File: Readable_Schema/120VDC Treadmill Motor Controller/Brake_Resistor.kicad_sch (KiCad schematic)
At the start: 11 parts, among them Q9 IPP200N25N3GXKSA1, U10 FOD3182, U11 TC75S56F_LF

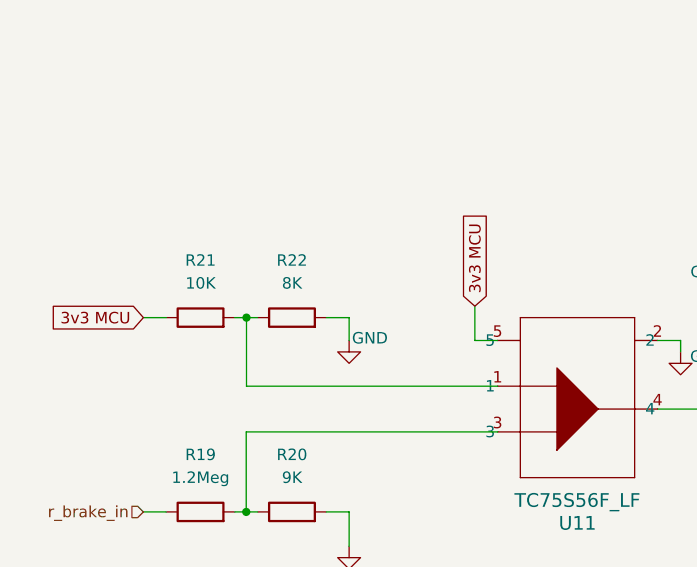
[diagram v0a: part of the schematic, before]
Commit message: realizing we want shared footprints for all resistors
-Double check to make sure all sub 1W resistors share a footprint
-Choose and size a actual brake resistor, we currently own 3x 4ohm 100w resistors, not sure if those would be sufficient
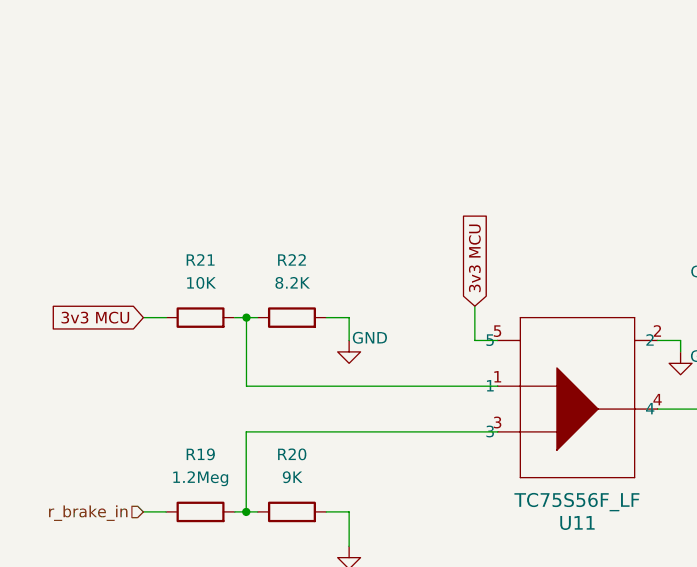
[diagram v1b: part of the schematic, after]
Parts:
- R19, R20, R21: footprint (none) -> Resistor_SMD:R_0201_0603Metric_Pad0.64x0.40mm_HandSolder
- R22: value 8K -> 8.2K; footprint (none) -> Resistor_SMD:R_0201_0603Metric_Pad0.64x0.40mm_HandSolder
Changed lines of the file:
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@@
 			)
 		)
-		(property "Footprint" ""
+		(property "Footprint" "Resistor_SMD:R_0201_0603Metric_Pad0.64x0.40mm_HandSolder"
 			(at 58.42 124.968 90)
 			(effects
@@
 			)
 		)
-		(property "Datasheet" "~"
+		(property "Datasheet" "https://industrial.panasonic.com/cdbs/www-data/pdf/RDA0000/AOA0000C301.pdf"
 			(at 58.42 123.19 0)
 			(effects
@@
 			)
 		)
-		(property "Description" "Resistor"
+		(property "Description" "ERJ-3GEYJ125V"
 			(at 58.42 123.19 0)
 			(effects
@@
 			)
 		)
-		(property "Footprint" ""
+		(property "Footprint" "Resistor_SMD:R_0201_0603Metric_Pad0.64x0.40mm_HandSolder"
 			(at 68.58 124.968 90)
 			(effects
@@
 			)
 		)
-		(property "Datasheet" "~"
+		(property "Datasheet" "https://industrial.panasonic.com/cdbs/www-data/pdf/RDA0000/AOA0000C304.pdf"
 			(at 68.58 123.19 0)
 			(effects
@@
 			)
 		)
-		(property "Description" "Resistor"
+		(property "Description" "ERJ-3EKF9091V"
 			(at 68.58 123.19 0)
 			(effects
@@
 			)
 		)
-		(property "Value" "8K"
+		(property "Value" "8.2K"
 			(at 68.58 97.79 90)
 			(effects
@@
 			)
 		)
-		(property "Footprint" ""
+		(property "Footprint" "Resistor_SMD:R_0201_0603Metric_Pad0.64x0.40mm_HandSolder"
 			(at 68.58 103.378 90)
 			(effects
@@
 			)
 		)
-		(property "Footprint" ""
+		(property "Footprint" "Resistor_SMD:R_0201_0603Metric_Pad0.64x0.40mm_HandSolder"
 			(at 58.42 103.378 90)
 			(effects
@@
 			)
 		)
-		(property "Description" "Resistor"
+		(property "Description" "ERJ-3GEYJ103V"
 			(at 58.42 101.6 0)
 			(effects

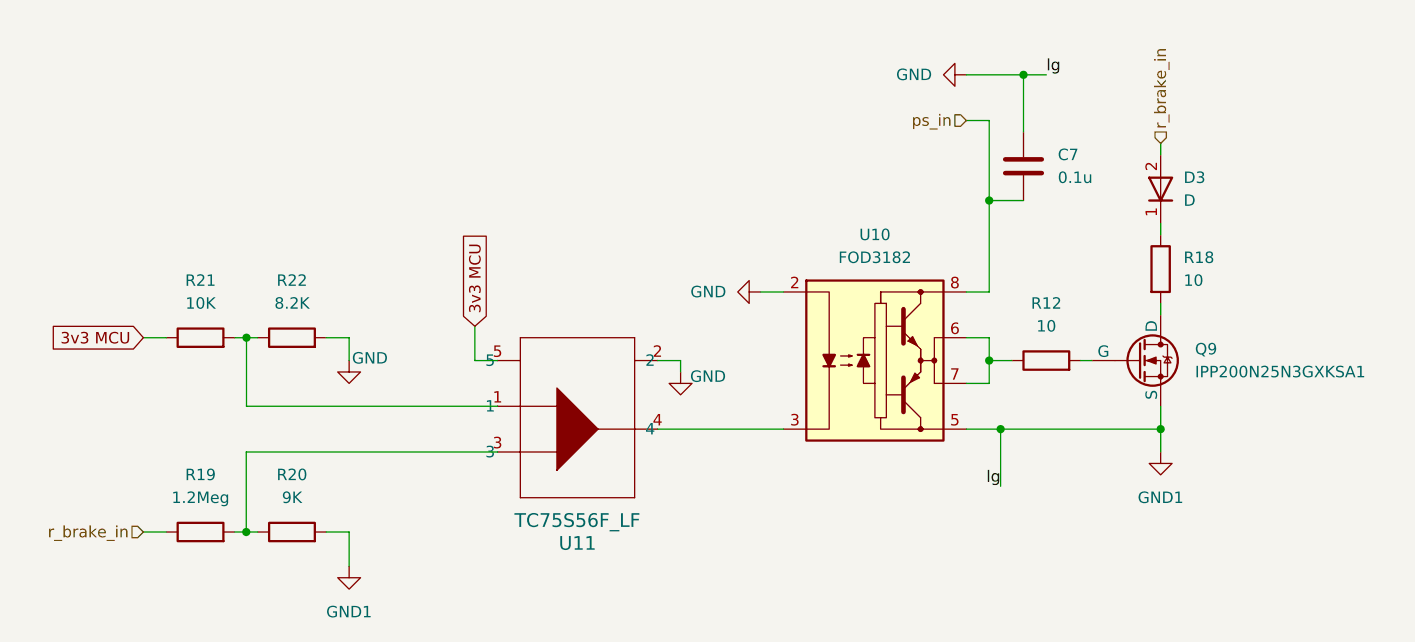
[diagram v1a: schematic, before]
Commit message: we have reached the point of starting to roughly place where components should go (have not started messing with traces). -Confirm heatsink size so that we can block that area out on the schema -add some test points similar to what we were testing in ltspice to determine functionality of the device -Review general layout with dad to confirm we r good to start drawing traces
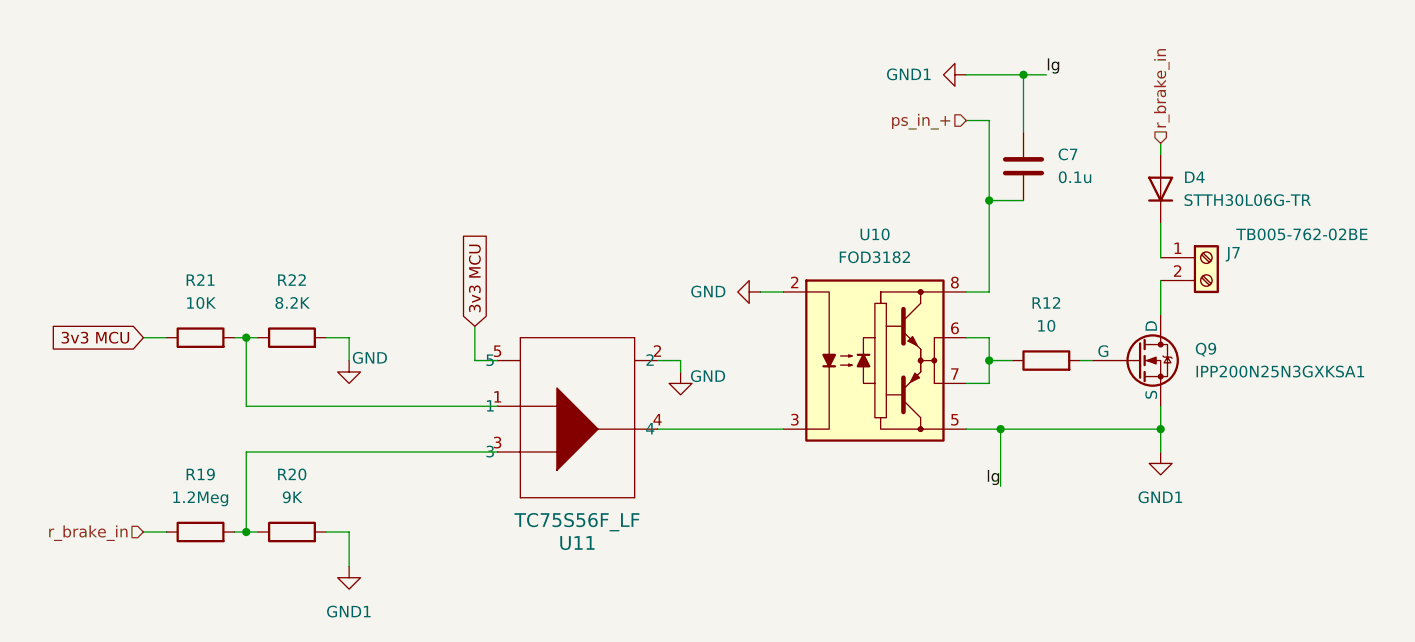
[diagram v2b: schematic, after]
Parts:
- removed D3: D, symbol Simulation_SPICE:D
- removed R18: 10, symbol Device:R
- added D4: STTH30L06G-TR, Package_TO_SOT_SMD:TO-263-2, symbol Diode:STTH2002G
- added J7: TB005-762-02BE, Treadmill_Feet:TB005-762-02BE_CUD, symbol Connector:Screw_Terminal_01x02
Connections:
- net GND: no longer C7.1, Q9.3 (S), R20.2, U10.5 (VEE)
- net r_brake_in: now also D4.3 (A)
- net at Q9.1 (D): now also J7.2 (Pin_2)
- net ps_in renamed ps_in_+
- new net: D4.2 (K), J7.1 (Pin_1)
- new net GND1: C7.1, Q9.3 (S), R20.2, U10.5 (VEE)

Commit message: Stretched out the pcb a bit to give me some more room to work with. -Missing something to prevent main cap from blowing up on startup
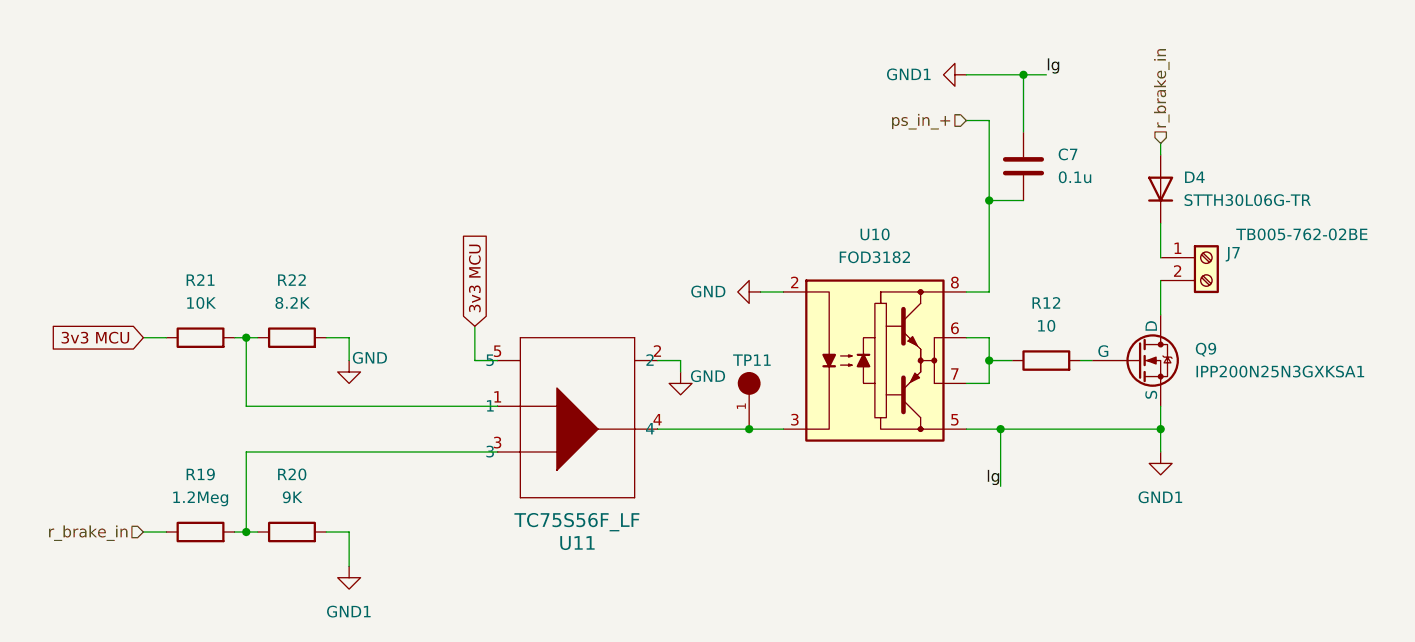
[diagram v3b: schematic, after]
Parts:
- added TP11: RCWCTE, Treadmill_Feet:RCWCTE, symbol Treadmill_Comp:RCWCTE
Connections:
- net at U10.3 (C), U11.4: now also TP11.1
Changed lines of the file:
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@@
+	)
+	(junction
+		(at 119.38 111.76)
+		(diameter 0)
+		(color 0 0 0 0)
 	)
 	(junction
@@
 	(wire
 		(pts
+			(xy 119.38 111.76) (xy 123.19 111.76)
+		)
+		(stroke
+			(width 0)
+			(type default)
+		)
+	)
+	(wire
+		(pts
 			(xy 63.5 101.6) (xy 64.77 101.6)
 		)
@@
 	(wire
 		(pts
-			(xy 109.22 111.76) (xy 123.19 111.76)
+			(xy 109.22 111.76) (xy 119.38 111.76)
 		)
 		(stroke
@@
 					(unit 1)
 				)
+			)
+		)
+	)
+	(symbol
+		(lib_id "Treadmill_Comp:RCWCTE")
+		(at 119.38 106.68 90)
+		(unit 1)
+		(exclude_from_sim no)
+		(in_bom yes)
+		(on_board yes)
+		(dnp no)
+		(property "Reference" "TP11"
+			(at 117.602 104.14 90)
+			(effects
+				(font
+					(size 1.27 1.27)
+				)
+				(justify right)
+			)
+		)
+		(property "Value" "RCWCTE"
+			(at 121.92 107.9499 90)
+			(effects
+				(font
+					(size 1.27 1.27)
+				)
+				(justify right)
+				(hide yes)
+			)
+		)
+		(property "Footprint" "Treadmill_Feet:RCWCTE"
+			(at 119.38 106.68 0)
+			(effects
+				(font
+					(size 1.27 1.27)
+				)
+				(justify bottom)
+				(hide yes)
+			)
+		)
+		(property "Datasheet" "https://www.koaspeer.com/pdfs/RC.pdf"
+			(at 119.38 106.68 0)
+			(effects
+				(font
+					(size 1.27 1.27)
+				)
+				(hide yes)
+			)
+		)
+		(property "Description" "https://www.digikey.com/en/products/detail/koa-speer-electronics-inc/RCWCTE/11476558"
+			(at 119.38 106.68 0)
+			(effects
+				(font
+					(size 1.27 1.27)
+				)
+				(hide yes)
+			)
+		)
+		(property "PARTREV" "1/06/14"
+			(at 119.38 106.68 0)
+			(effects
+				(font
+					(size 1.27 1.27)
+				)
+				(justify bottom)
+				(hide yes)
+			)
+		)
+		(property "SNAPEDA_PN" "RCWCTE"
+			(at 119.38 106.68 0)
+			(effects
+				(font
+					(size 1.27 1.27)
+				)
+				(justify bottom)
+				(hide yes)
+			)
+		)
+		(property "MANUFACTURER" "KOA Speer"
+			(at 119.38 106.68 0)
+			(effects
+				(font
+					(size 1.27 1.27)
+				)
+				(justify bottom)
+				(hide yes)
+			)
+		)
+		(property "MAXIMUM_PACKAGE_HEIGHT" "2 mm"
+			(at 119.38 106.68 0)
+			(effects
+				(font
+					(size 1.27 1.27)
+				)
+				(justify bottom)
+				(hide yes)
+			)
+		)
+		(property "STANDARD" "Manufacturer Recommendations"
+			(at 119.38 106.68 0)
+			(effects
+				(font
+					(size 1.27 1.27)
+				)
+				(justify bottom)
+				(hide yes)
+			)
+		)
+		(pin "1"
+		)
+		(instances
+			(project "120VDC Treadmill Motor Controller"
+				(path "/319bc5c0-2dd5-4df3-a34b-9170833ebccd/7a7487b9-35f1-42d2-9ba5-cfe8e231a0f8"
+					(reference "TP11")
+					(unit 1)
+				)

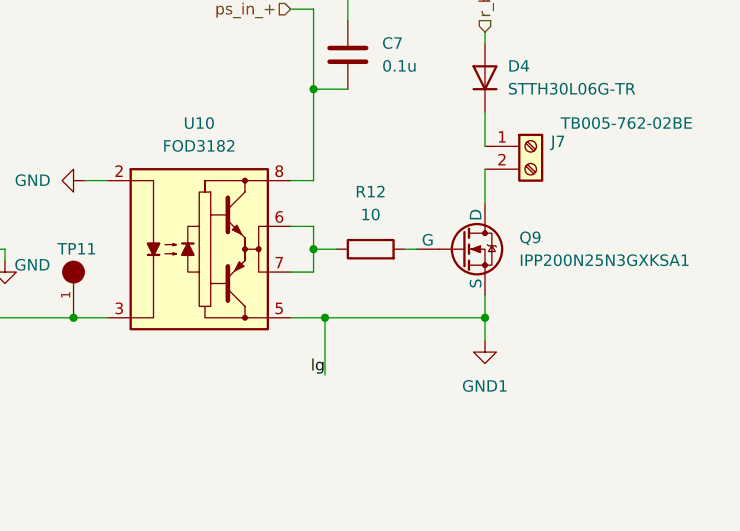
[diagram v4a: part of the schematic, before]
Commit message: Finished choosing real components for the digitally isolated drives. Mainly followed TIs 100khz example and chose to use mostly repeat components. Now confirming the design doesnt suck then working on traces
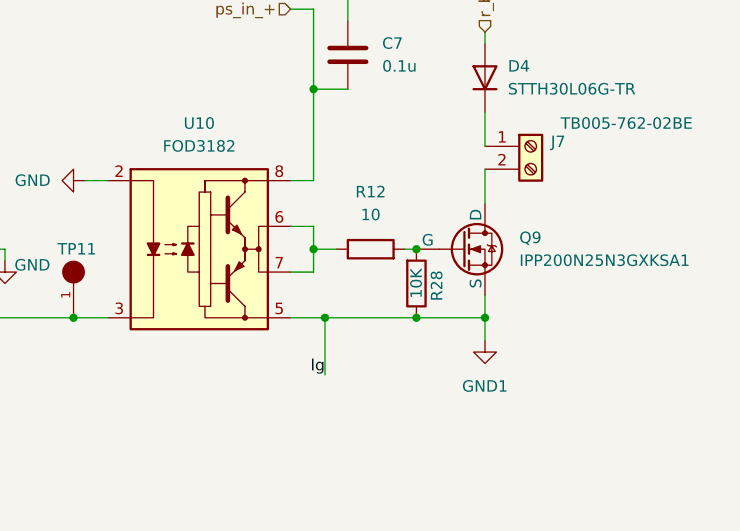
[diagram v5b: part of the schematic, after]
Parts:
- added R28: 10K, Resistor_SMD:R_0201_0603Metric_Pad0.64x0.40mm_HandSolder, symbol Device:R
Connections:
- net GND1: now also R28.1
- net at Q9.2 (G), R12.2: now also R28.2
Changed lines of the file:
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@@
 	(paper "A4")
 	(junction
+		(at 157.48 104.14)
+		(diameter 0)
+		(color 0 0 0 0)
+	)
+	(junction
 		(at 63.5 101.6)
 		(diameter 0)
@@
 	)
 	(junction
+		(at 157.48 111.76)
+		(diameter 0)
+		(color 0 0 0 0)
+	)
+	(junction
 		(at 149.86 72.39)
 		(diameter 0)
@@
 	(wire
 		(pts
-			(xy 147.32 111.76) (xy 165.1 111.76)
+			(xy 147.32 111.76) (xy 157.48 111.76)
 		)
 		(stroke
@@
 		(pts
 			(xy 63.5 123.19) (xy 64.77 123.19)
+		)
+		(stroke
+			(width 0)
+			(type default)
+		)
+	)
+	(wire
+		(pts
+			(xy 157.48 111.76) (xy 165.1 111.76)
 		)
 		(stroke
@@
 					(unit 1)
 				)
+			)
+		)
+	)
+	(symbol
+		(lib_id "Device:R")
+		(at 157.48 107.95 0)
+		(mirror x)
+		(unit 1)
+		(exclude_from_sim no)
+		(in_bom yes)
+		(on_board yes)
+		(dnp no)
+		(property "Reference" "R28"
+			(at 159.766 108.204 90)
+			(effects
+				(font
+					(size 1.27 1.27)
+				)
+			)
+		)
+		(property "Value" "10K"
+			(at 157.48 107.95 90)
+			(effects
+				(font
+					(size 1.27 1.27)
+				)
+			)
+		)
+		(property "Footprint" "Resistor_SMD:R_0201_0603Metric_Pad0.64x0.40mm_HandSolder"
+			(at 155.702 107.95 90)
+			(effects
+				(font
+					(size 1.27 1.27)
+				)
+				(hide yes)
+			)
+		)
+		(property "Datasheet" "https://industrial.panasonic.com/cdbs/www-data/pdf/RDP0000/AOA0000C337.pdf"
+			(at 157.48 107.95 0)
+			(effects
+				(font
+					(size 1.27 1.27)
+				)
+				(hide yes)
+			)
+		)
+		(property "Description" "ERJ-UP3J100V"
+			(at 157.48 107.95 0)
+			(effects
+				(font
+					(size 1.27 1.27)
+				)
+				(hide yes)
+			)
+		)
+		(pin "1"
+		)
+		(pin "2"
+		)
+		(instances
+			(project "120VDC Treadmill Motor Controller"
+				(path "/319bc5c0-2dd5-4df3-a34b-9170833ebccd/7a7487b9-35f1-42d2-9ba5-cfe8e231a0f8"
+					(reference "R28")
+					(unit 1)
+				)

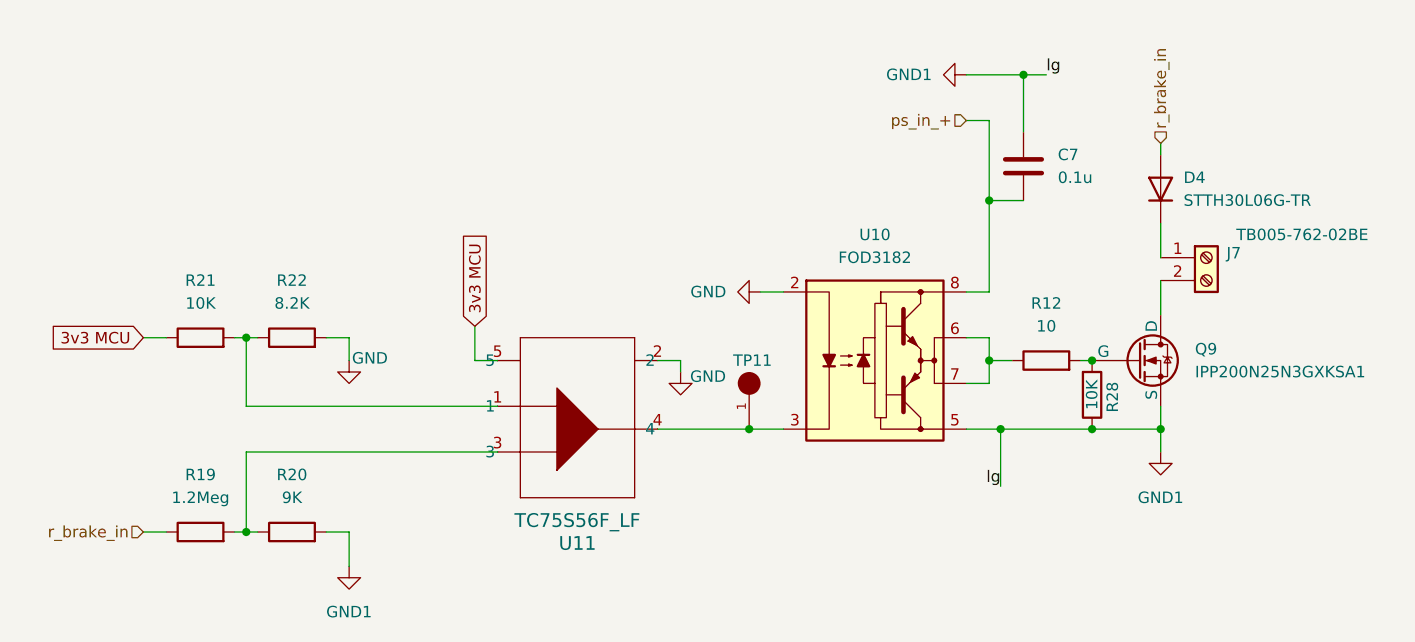
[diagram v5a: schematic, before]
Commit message: Changed ground naming and redid a bit of the pinouts between the pico and the h bridge -- need to fix the feedback loop to use a or gate for pwm_a and pwm_b to combine to one big reset
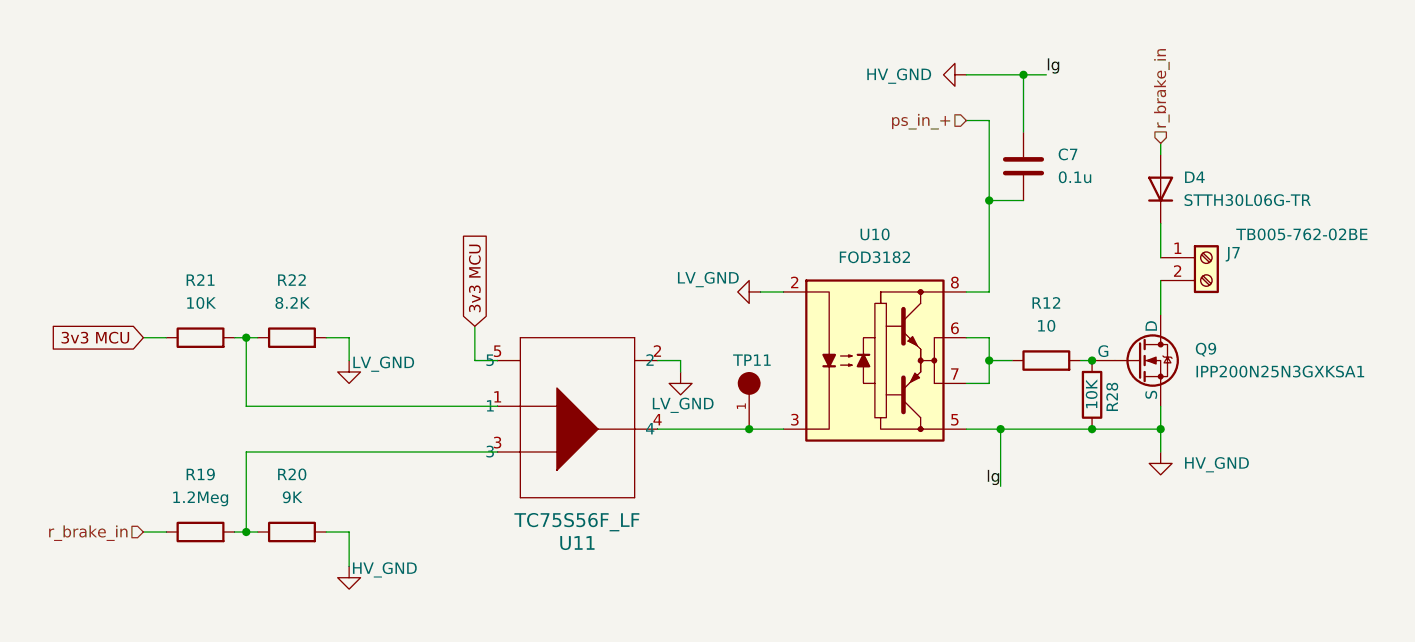
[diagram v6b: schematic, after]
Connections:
- net GND renamed LV_GND
- net GND1 renamed HV_GND
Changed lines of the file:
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@@
 			)
 		)
-		(property "Value" "GND1"
+		(property "Value" "HV_GND"
 			(at 139.7 72.3899 90)
 			(effects
@@
 			)
 		)
-		(property "Value" "GND"
-			(at 77.2414 103.886 0)
+		(property "Value" "LV_GND"
+			(at 78.74 104.394 0)
 			(effects
 				(font
@@
 			)
 		)
-		(property "Value" "GND"
-			(at 114.808 105.918 0)
+		(property "Value" "LV_GND"
+			(at 112.014 108.966 0)
 			(effects
 				(font
@@
 			)
 		)
-		(property "Value" "GND1"
-			(at 165.1 119.38 0)
-			(effects
-				(font
-					(size 1.27 1.27)
-				)
+		(property "Value" "HV_GND"
+			(at 167.64 115.5699 0)
+			(effects
+				(font
+					(size 1.27 1.27)
+				)
+				(justify left)
 			)
 		)
@@
 		(on_board yes)
 		(dnp no)
-		(fields_autoplaced yes)
 		(property "Reference" "#PWR033"
 			(at 114.3 96.52 0)
@@
 			)
 		)
-		(property "Value" "GND"
-			(at 116.84 96.5199 90)
-			(effects
-				(font
-					(size 1.27 1.27)
-				)
-				(justify right)
+		(property "Value" "LV_GND"
+			(at 114.808 94.996 90)
+			(effects
+				(font
+					(size 1.27 1.27)
+				)
 			)
 		)
@@
 		(on_board yes)
 		(dnp no)
-		(fields_autoplaced yes)
 		(property "Reference" "#PWR036"
 			(at 74.93 133.35 0)
@@
 			)
 		)
-		(property "Value" "GND1"
-			(at 74.93 132.08 0)
-			(effects
-				(font
-					(size 1.27 1.27)
-				)
-			)
-		)
+		(property "Value" "HV_GND"
+			(at 75.184 127.254 0)
+			(effects
+				(font
+					(size 1.27 1.27)
+				)
+				(justify left)
+			)
+		)
